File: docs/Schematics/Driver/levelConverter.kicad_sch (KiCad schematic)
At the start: 2 parts

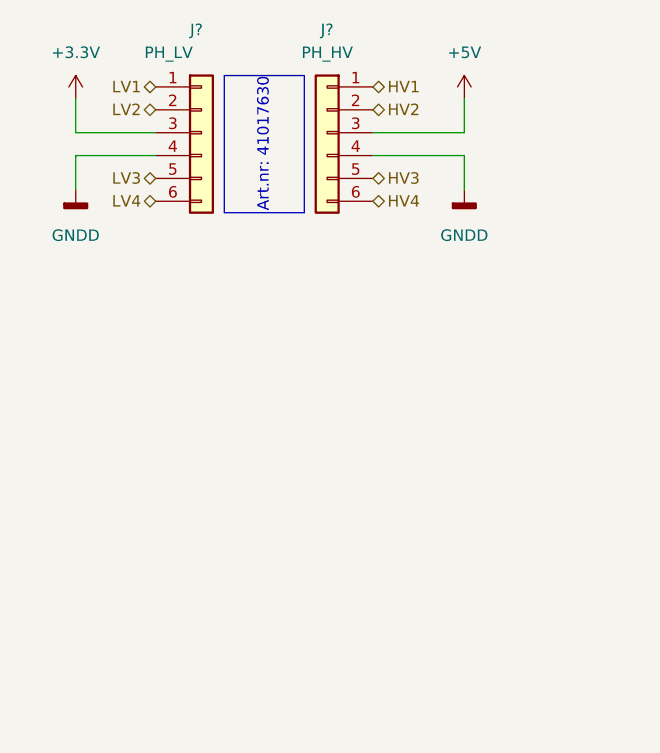
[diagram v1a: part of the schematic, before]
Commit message: Added footprints and a symbol for the level shifters
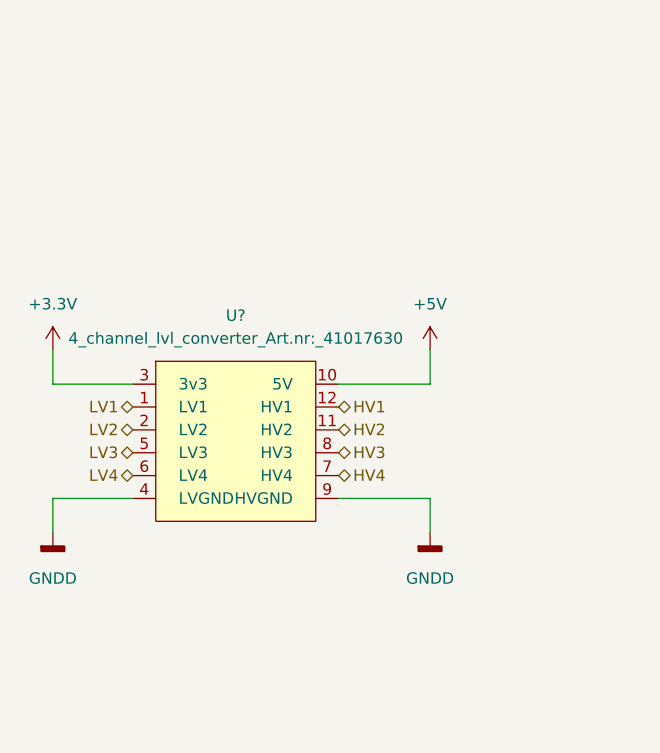
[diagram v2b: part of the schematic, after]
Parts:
- removed J?: PH_LV, symbol Connector_Generic:Conn_01x06
- removed J?: PH_HV, symbol Connector_Generic:Conn_01x06
- added U?: 4_channel_lvl_converter_Art.nr:_41017630, project:4ch_level_shifter_Artnr_ 41017630, symbol project:4_channel_lvl_converter_Art.nr{colon}_41017630
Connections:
- net +3.3V: now also U?.3 (3v3)
- net +5V: now also U?.10 (5V)
- net GNDD: now also U?.4 (LVGND), U?.9 (HVGND)
- net HV1: now also U?.12 (HV1)
- net HV2: now also U?.11 (HV2)
- net HV3: now also U?.8 (HV3)
- net HV4: now also U?.7 (HV4)
- net LV1: now also U?.1 (LV1)
- net LV2: now also U?.2 (LV2)
- net LV3: now also U?.5 (LV3)
- net LV4: now also U?.6 (LV4)
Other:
- note removed: "Art.nr: 41017630"
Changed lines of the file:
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@@
     (company "HiQ")
   )
-  (wire (pts (xy 135.89 77.47) (xy 135.89 81.28))
+  (wire (pts (xy 133.35 115.57) (xy 133.35 119.38))
     (stroke (width 0) (type default) (color 0 0 0 0))
   )
-  (polyline (pts (xy 152.4 68.58) (xy 152.4 83.82))
+  (wire (pts (xy 133.35 99.06) (xy 133.35 102.87))
     (stroke (width 0) (type default) (color 0 0 0 0))
   )
-  (wire (pts (xy 135.89 71.12) (xy 135.89 74.93))
+  (wire (pts (xy 165.1 102.87) (xy 175.26 102.87))
     (stroke (width 0) (type default) (color 0 0 0 0))
   )
-  (wire (pts (xy 168.91 74.93) (xy 179.07 74.93))
+  (wire (pts (xy 133.35 102.87) (xy 142.24 102.87))
     (stroke (width 0) (type default) (color 0 0 0 0))
   )
-  (wire (pts (xy 135.89 74.93) (xy 144.78 74.93))
+  (wire (pts (xy 165.1 115.57) (xy 175.26 115.57))
     (stroke (width 0) (type default) (color 0 0 0 0))
   )
-  (polyline (pts (xy 161.29 68.58) (xy 161.29 83.82))
+  (wire (pts (xy 175.26 115.57) (xy 175.26 119.38))
     (stroke (width 0) (type default) (color 0 0 0 0))
   )
-  (polyline (pts (xy 161.29 83.82) (xy 152.4 83.82))
+  (wire (pts (xy 142.24 115.57) (xy 133.35 115.57))
     (stroke (width 0) (type default) (color 0 0 0 0))
   )
-  (polyline (pts (xy 152.4 68.58) (xy 161.29 68.58))
-    (stroke (width 0) (type default) (color 0 0 0 0))
-  )
-  (wire (pts (xy 168.91 77.47) (xy 179.07 77.47))
-    (stroke (width 0) (type default) (color 0 0 0 0))
-  )
-  (wire (pts (xy 179.07 77.47) (xy 179.07 81.28))
-    (stroke (width 0) (type default) (color 0 0 0 0))
-  )
-  (wire (pts (xy 144.78 77.47) (xy 135.89 77.47))
-    (stroke (width 0) (type default) (color 0 0 0 0))
-  )
-  (wire (pts (xy 179.07 74.93) (xy 179.07 71.12))
+  (wire (pts (xy 175.26 102.87) (xy 175.26 99.06))
     (stroke (width 0) (type default) (color 0 0 0 0))
   )
@@
     (effects (font (size 1.27 1.27)) (justify left bottom))
   )
-  (text "Art.nr: 41017630" (at 157.48 83.82 90)
-    (effects (font (size 1.27 1.27)) (justify left bottom))
-  )
-  (hierarchical_label "LV4" (shape bidirectional) (at 144.78 82.55 180)
+  (hierarchical_label "LV4" (shape bidirectional) (at 142.24 113.03 180)
     (effects (font (size 1.27 1.27)) (justify right))
   )
-  (hierarchical_label "HV2" (shape bidirectional) (at 168.91 72.39 0)
+  (hierarchical_label "HV2" (shape bidirectional) (at 165.1 107.95 0)
     (effects (font (size 1.27 1.27)) (justify left))
   )
-  (hierarchical_label "HV1" (shape bidirectional) (at 168.91 69.85 0)
+  (hierarchical_label "HV1" (shape bidirectional) (at 165.1 105.41 0)
     (effects (font (size 1.27 1.27)) (justify left))
   )
-  (hierarchical_label "HV3" (shape bidirectional) (at 168.91 80.01 0)
+  (hierarchical_label "HV3" (shape bidirectional) (at 165.1 110.49 0)
     (effects (font (size 1.27 1.27)) (justify left))
   )
-  (hierarchical_label "HV4" (shape bidirectional) (at 168.91 82.55 0)
+  (hierarchical_label "HV4" (shape bidirectional) (at 165.1 113.03 0)
     (effects (font (size 1.27 1.27)) (justify left))
   )
-  (hierarchical_label "LV2" (shape bidirectional) (at 144.78 72.39 180)
+  (hierarchical_label "LV2" (shape bidirectional) (at 142.24 107.95 180)
     (effects (font (size 1.27 1.27)) (justify right))
   )
-  (hierarchical_label "LV3" (shape bidirectional) (at 144.78 80.01 180)
+  (hierarchical_label "LV3" (shape bidirectional) (at 142.24 110.49 180)
     (effects (font (size 1.27 1.27)) (justify right))
   )
-  (hierarchical_label "LV1" (shape bidirectional) (at 144.78 69.85 180)
+  (hierarchical_label "LV1" (shape bidirectional) (at 142.24 105.41 180)
     (effects (font (size 1.27 1.27)) (justify right))
   )
-  (symbol (lib_id "power:+3.3V") (at 135.89 71.12 0) (unit 1)
+  (symbol (lib_id "power:+3.3V") (at 133.35 99.06 0) (unit 1)
     (in_bom yes) (on_board yes) (fields_autoplaced)
-    (property "Reference" "#PWR?" (id 0) (at 135.89 74.93 0)
+    (property "Reference" "#PWR01" (id 0) (at 133.35 102.87 0)
       (effects (font (size 1.27 1.27)) hide)
     )
-    (property "Value" "+3.3V" (id 1) (at 135.89 66.04 0))
-    (property "Footprint" "" (id 2) (at 135.89 71.12 0)
+    (property "Value" "+3.3V" (id 1) (at 133.35 93.98 0))
+    (property "Footprint" "" (id 2) (at 133.35 99.06 0)
       (effects (font (size 1.27 1.27)) hide)
     )
-    (property "Datasheet" "" (id 3) (at 135.89 71.12 0)
+    (property "Datasheet" "" (id 3) (at 133.35 99.06 0)
       (effects (font (size 1.27 1.27)) hide)
     )
     (pin "1")
   )
-  (symbol (lib_id "power:+5V") (at 179.07 71.12 0) (unit 1)
+  (symbol (lib_id "power:+5V") (at 175.26 99.06 0) (unit 1)
     (in_bom yes) (on_board yes) (fields_autoplaced)
-    (property "Reference" "#PWR?" (id 0) (at 179.07 74.93 0)
+    (property "Reference" "#PWR03" (id 0) (at 175.26 102.87 0)
       (effects (font (size 1.27 1.27)) hide)
     )
-    (property "Value" "+5V" (id 1) (at 179.07 66.04 0))
-    (property "Footprint" "" (id 2) (at 179.07 71.12 0)
+    (property "Value" "+5V" (id 1) (at 175.26 93.98 0))
+    (property "Footprint" "" (id 2) (at 175.26 99.06 0)
       (effects (font (size 1.27 1.27)) hide)
     )
-    (property "Datasheet" "" (id 3) (at 179.07 71.12 0)
+    (property "Datasheet" "" (id 3) (at 175.26 99.06 0)
       (effects (font (size 1.27 1.27)) hide)
     )
     (pin "1")
   )
-  (symbol (lib_id "Connector_Generic:Conn_01x06") (at 149.86 74.93 0) (unit 1)
-    (in_bom yes) (on_board yes)
-    (property "Reference" "J?" (id 0) (at 148.59 63.5 0)
-      (effects (font (size 1.27 1.27)) (justify left))
-    )
-    (property "Value" "PH_LV" (id 1) (at 143.51 66.04 0)
-      (effects (font (size 1.27 1.27)) (justify left))
-    )
-    (property "Footprint" "" (id 2) (at 149.86 74.93 0)
+  (symbol (lib_id "power:GNDD") (at 133.35 119.38 0) (unit 1)
+    (in_bom yes) (on_board yes) (fields_autoplaced)
+    (property "Reference" "#PWR02" (id 0) (at 133.35 125.73 0)
       (effects (font (size 1.27 1.27)) hide)
     )
-    (property "Datasheet" "~" (id 3) (at 149.86 74.93 0)
+    (property "Value" "GNDD" (id 1) (at 133.35 124.46 0))
+    (property "Footprint" "" (id 2) (at 133.35 119.38 0)
+      (effects (font (size 1.27 1.27)) hide)
+    )
+    (property "Datasheet" "" (id 3) (at 133.35 119.38 0)
       (effects (font (size 1.27 1.27)) hide)
     )
     (pin "1")
+  )
+  (symbol (lib_id "project:4_channel_lvl_converter_Art.nr{colon}_41017630") (at 153.67 109.22 0) (unit 1)
+    (in_bom yes) (on_board yes) (fields_autoplaced)
+    (property "Reference" "U?" (id 0) (at 153.67 95.25 0))
+    (property "Value" "4_channel_lvl_converter_Art.nr:_41017630" (id 1) (at 153.67 97.79 0))
+    (property "Footprint" "project:4ch_level_shifter_Artnr_ 41017630" (id 2) (at 142.24 105.41 0)
+      (effects (font (size 1.27 1.27)) hide)
+    )
+    (property "Datasheet" "" (id 3) (at 142.24 105.41 0)
+      (effects (font (size 1.27 1.27)) hide)
+    )
+    (pin "1")
+    (pin "10")
+    (pin "11")
+    (pin "12")
     (pin "2")
     (pin "3")
@@
     (pin "5")
     (pin "6")
+    (pin "7")
+    (pin "8")
+    (pin "9")
   )
-  (symbol (lib_id "power:GNDD") (at 135.89 81.28 0) (unit 1)
+  (symbol (lib_id "power:GNDD") (at 175.26 119.38 0) (unit 1)
     (in_bom yes) (on_board yes) (fields_autoplaced)
-    (property "Reference" "#PWR?" (id 0) (at 135.89 87.63 0)
+    (property "Reference" "#PWR04" (id 0) (at 175.26 125.73 0)
       (effects (font (size 1.27 1.27)) hide)
     )
-    (property "Value" "GNDD" (id 1) (at 135.89 86.36 0))
-    (property "Footprint" "" (id 2) (at 135.89 81.28 0)
+    (property "Value" "GNDD" (id 1) (at 175.26 124.46 0))
+    (property "Footprint" "" (id 2) (at 175.26 119.38 0)
       (effects (font (size 1.27 1.27)) hide)
     )
-    (property "Datasheet" "" (id 3) (at 135.89 81.28 0)
+    (property "Datasheet" "" (id 3) (at 175.26 119.38 0)
       (effects (font (size 1.27 1.27)) hide)
     )
-    (pin "1")
-  )
-  (symbol (lib_id "Connector_Generic:Conn_01x06") (at 163.83 74.93 0) (mirror y) (unit 1)
-    (in_bom yes) (on_board yes) (fields_autoplaced)
-    (property "Reference" "J?" (id 0) (at 163.83 63.5 0))
-    (property "Value" "PH_HV" (id 1) (at 163.83 66.04 0))
-    (property "Footprint" "" (id 2) (at 163.83 74.93 0)
-      (effects (font (size 1.27 1.27)) hide)
-    )
-    (property "Datasheet" "~" (id 3) (at 163.83 74.93 0)
-      (effects (font (size 1.27 1.27)) hide)
-    )
-    (pin "1")
-    (pin "2")
-    (pin "3")
-    (pin "4")
-    (pin "5")
-    (pin "6")
-  )
-  (symbol (lib_id "power:GNDD") (at 179.07 81.28 0) (unit 1)
-    (in_bom yes) (on_board yes) (fields_autoplaced)
-    (property "Reference" "#PWR?" (id 0) (at 179.07 87.63 0)
-      (effects (font (size 1.27 1.27)) hide)
-    )
-    (property "Value" "GNDD" (id 1) (at 179.07 86.36 0))
-    (property "Footprint" "" (id 2) (at 179.07 81.28 0)
-      (effects (font (size 1.27 1.27)) hide)
-    )
-    (property "Datasheet" "" (id 3) (at 179.07 81.28 0)
-      (effects (font (size 1.27 1.27)) hide)
-    )

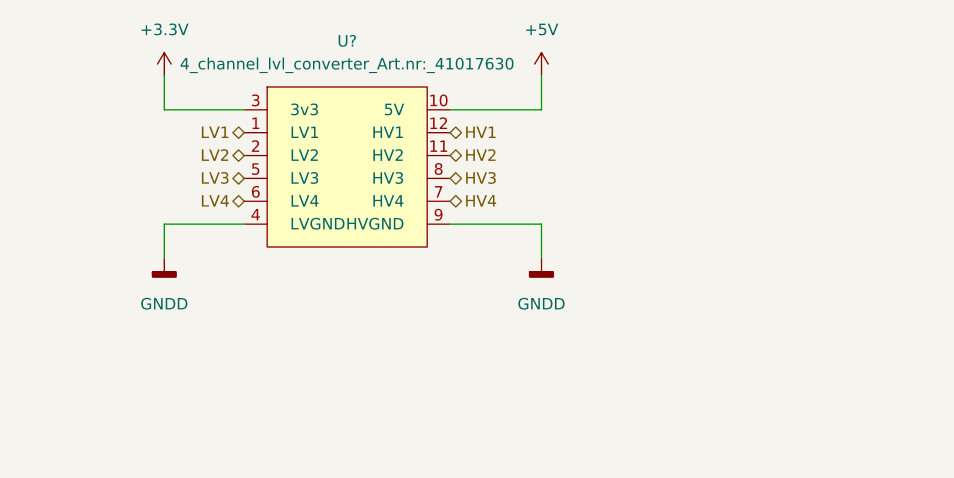
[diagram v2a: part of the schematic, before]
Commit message: Added caps and changed the connection from the motor sensors to plints
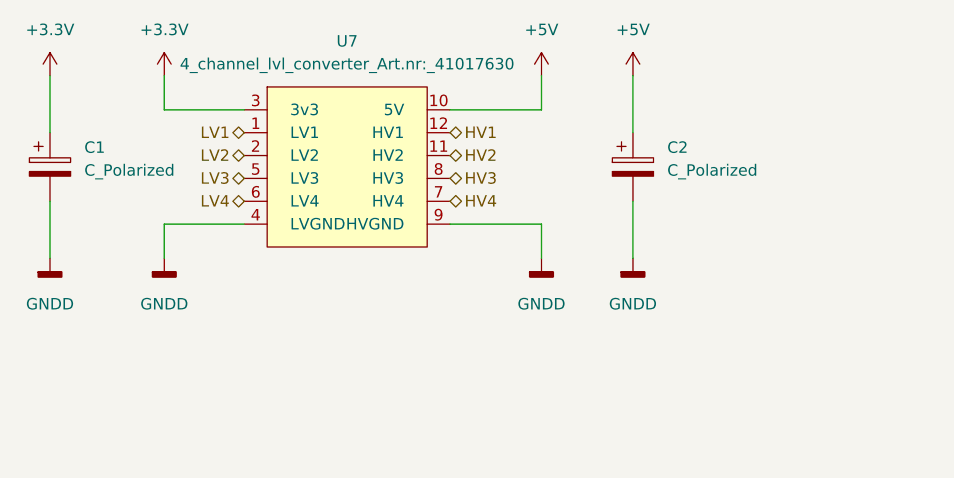
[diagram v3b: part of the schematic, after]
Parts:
- added C1, C2: C_Polarized, Capacitor_THT:CP_Radial_D6.3mm_P2.50mm, symbol Device:C_Polarized
- gave numbers to parts that had none: 1
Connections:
- net +3.3V: now also C1.1
- net +5V: now also C2.1
- net GNDD: now also C1.2, C2.2
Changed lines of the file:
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@@
+    (stroke (width 0) (type default) (color 0 0 0 0))
+  )
+  (wire (pts (xy 120.65 113.03) (xy 120.65 119.38))
     (stroke (width 0) (type default) (color 0 0 0 0))
   )
@@
     (stroke (width 0) (type default) (color 0 0 0 0))
   )
+  (wire (pts (xy 185.42 99.06) (xy 185.42 105.41))
+    (stroke (width 0) (type default) (color 0 0 0 0))
+  )
+  (wire (pts (xy 185.42 113.03) (xy 185.42 119.38))
+    (stroke (width 0) (type default) (color 0 0 0 0))
+  )
   (wire (pts (xy 175.26 102.87) (xy 175.26 99.06))
+    (stroke (width 0) (type default) (color 0 0 0 0))
+  )
+  (wire (pts (xy 120.65 99.06) (xy 120.65 105.41))
     (stroke (width 0) (type default) (color 0 0 0 0))
   )
@@
     (effects (font (size 1.27 1.27)) (justify right))
   )
+  (symbol (lib_id "Device:C_Polarized") (at 120.65 109.22 0) (unit 1)
+    (in_bom yes) (on_board yes) (fields_autoplaced)
+    (property "Reference" "C1" (id 0) (at 124.46 107.0609 0)
+      (effects (font (size 1.27 1.27)) (justify left))
+    )
+    (property "Value" "C_Polarized" (id 1) (at 124.46 109.6009 0)
+      (effects (font (size 1.27 1.27)) (justify left))
+    )
+    (property "Footprint" "Capacitor_THT:CP_Radial_D6.3mm_P2.50mm" (id 2) (at 121.6152 113.03 0)
+      (effects (font (size 1.27 1.27)) hide)
+    )
+    (property "Datasheet" "~" (id 3) (at 120.65 109.22 0)
+      (effects (font (size 1.27 1.27)) hide)
+    )
+    (pin "1")
+    (pin "2")
+  )
   (symbol (lib_id "power:+3.3V") (at 133.35 99.06 0) (unit 1)
     (in_bom yes) (on_board yes) (fields_autoplaced)
@@
     (pin "1")
   )
+  (symbol (lib_id "power:GNDD") (at 120.65 119.38 0) (unit 1)
+    (in_bom yes) (on_board yes) (fields_autoplaced)
+    (property "Reference" "#PWR040" (id 0) (at 120.65 125.73 0)
+      (effects (font (size 1.27 1.27)) hide)
+    )
+    (property "Value" "GNDD" (id 1) (at 120.65 124.46 0))
+    (property "Footprint" "" (id 2) (at 120.65 119.38 0)
+      (effects (font (size 1.27 1.27)) hide)
+    )
+    (property "Datasheet" "" (id 3) (at 120.65 119.38 0)
+      (effects (font (size 1.27 1.27)) hide)
+    )
+    (pin "1")
+  )
   (symbol (lib_id "power:GNDD") (at 133.35 119.38 0) (unit 1)
     (in_bom yes) (on_board yes) (fields_autoplaced)
@@
     (pin "1")
   )
+  (symbol (lib_id "power:+3.3V") (at 120.65 99.06 0) (unit 1)
+    (in_bom yes) (on_board yes) (fields_autoplaced)
+    (property "Reference" "#PWR039" (id 0) (at 120.65 102.87 0)
+      (effects (font (size 1.27 1.27)) hide)
+    )
+    (property "Value" "+3.3V" (id 1) (at 120.65 93.98 0))
+    (property "Footprint" "" (id 2) (at 120.65 99.06 0)
+      (effects (font (size 1.27 1.27)) hide)
+    )
+    (property "Datasheet" "" (id 3) (at 120.65 99.06 0)
+      (effects (font (size 1.27 1.27)) hide)
+    )
+    (pin "1")
+  )
+  (symbol (lib_id "Device:C_Polarized") (at 185.42 109.22 0) (unit 1)
+    (in_bom yes) (on_board yes)
+    (property "Reference" "C2" (id 0) (at 189.23 107.0609 0)
+      (effects (font (size 1.27 1.27)) (justify left))
+    )
+    (property "Value" "C_Polarized" (id 1) (at 189.23 109.6009 0)
+      (effects (font (size 1.27 1.27)) (justify left))
+    )
+    (property "Footprint" "Capacitor_THT:CP_Radial_D6.3mm_P2.50mm" (id 2) (at 186.3852 113.03 0)
+      (effects (font (size 1.27 1.27)) hide)
+    )
+    (property "Datasheet" "~" (id 3) (at 185.42 109.22 0)
+      (effects (font (size 1.27 1.27)) hide)
+    )
+    (pin "1")
+    (pin "2")
+  )
+  (symbol (lib_id "power:+5V") (at 185.42 99.06 0) (unit 1)
+    (in_bom yes) (on_board yes) (fields_autoplaced)
+    (property "Reference" "#PWR041" (id 0) (at 185.42 102.87 0)
+      (effects (font (size 1.27 1.27)) hide)
+    )
+    (property "Value" "+5V" (id 1) (at 185.42 93.98 0))
+    (property "Footprint" "" (id 2) (at 185.42 99.06 0)
+      (effects (font (size 1.27 1.27)) hide)
+    )
+    (property "Datasheet" "" (id 3) (at 185.42 99.06 0)
+      (effects (font (size 1.27 1.27)) hide)
+    )
+    (pin "1")
+  )
   (symbol (lib_id "project:4_channel_lvl_converter_Art.nr{colon}_41017630") (at 153.67 109.22 0) (unit 1)
     (in_bom yes) (on_board yes) (fields_autoplaced)
-    (property "Reference" "U?" (id 0) (at 153.67 95.25 0))
+    (property "Reference" "U7" (id 0) (at 153.67 95.25 0))
     (property "Value" "4_channel_lvl_converter_Art.nr:_41017630" (id 1) (at 153.67 97.79 0))
     (property "Footprint" "project:4ch_level_shifter_Artnr_ 41017630" (id 2) (at 142.24 105.41 0)
@@
     (pin "9")
   )
+  (symbol (lib_id "power:GNDD") (at 185.42 119.38 0) (unit 1)
+    (in_bom yes) (on_board yes) (fields_autoplaced)
+    (property "Reference" "#PWR042" (id 0) (at 185.42 125.73 0)
+      (effects (font (size 1.27 1.27)) hide)
+    )
+    (property "Value" "GNDD" (id 1) (at 185.42 124.46 0))
+    (property "Footprint" "" (id 2) (at 185.42 119.38 0)
+      (effects (font (size 1.27 1.27)) hide)
+    )
+    (property "Datasheet" "" (id 3) (at 185.42 119.38 0)
+      (effects (font (size 1.27 1.27)) hide)
+    )
+    (pin "1")
+  )
   (symbol (lib_id "power:GNDD") (at 175.26 119.38 0) (unit 1)

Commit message: Started routing the pcb.
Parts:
- C1, C2: footprint Capacitor_THT:CP_Radial_D6.3mm_P2.50mm -> Capacitor_SMD:C_0805_2012Metric_Pad1.18x1.45mm_HandSolder
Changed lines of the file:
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@@
       (effects (font (size 1.27 1.27)) (justify left))
     )
-    (property "Footprint" "Capacitor_THT:CP_Radial_D6.3mm_P2.50mm" (id 2) (at 121.6152 113.03 0)
+    (property "Footprint" "Capacitor_SMD:C_0805_2012Metric_Pad1.18x1.45mm_HandSolder" (id 2) (at 121.6152 113.03 0)
       (effects (font (size 1.27 1.27)) hide)
     )
@@
       (effects (font (size 1.27 1.27)) (justify left))
     )
-    (property "Footprint" "Capacitor_THT:CP_Radial_D6.3mm_P2.50mm" (id 2) (at 186.3852 113.03 0)
+    (property "Footprint" "Capacitor_SMD:C_0805_2012Metric_Pad1.18x1.45mm_HandSolder" (id 2) (at 186.3852 113.03 0)
       (effects (font (size 1.27 1.27)) hide)
     )

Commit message: First version of the routed board is done
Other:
- title: Arty Z7 IO expander card -> Arty Z7 IO Board
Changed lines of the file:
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@@
   (paper "A4")
   (title_block
-    (title "Arty Z7 IO expander card")
+    (title "Arty Z7 IO Board")
     (date "2022-12-24")
-    (rev "0.1")
+    (rev "${VER}")
     (company "HiQ")
   )
